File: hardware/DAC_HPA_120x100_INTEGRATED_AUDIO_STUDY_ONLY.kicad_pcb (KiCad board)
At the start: 4 copper layers, 120 x 100 mm, 544 parts, among them J101 GCT USB4105-GF-A, J201 PCB pads (no component), J202 PCB pads (no component), J701 G-Switch GT-3321667P-01, J702 HRO PJ-332A-6A, K601 TLP3545A, K602 TLP3545A, K603 TLP3545A, K604 TLP3545A, Q207 AO3400A, Q502 AO3400A, Q503 AO3400A, Q504 AO3400A, Q505 AO3400A, Q506 AO3400A, Q507 MMBT3904, Q612 MMBT3904, Q614 MMBT3904, Q616 AO3400A, Q617 AO3400A, Q618 2N7002, Q619 AO3400A, Q620 AO3400A, Q621 2N7002, Q622 AO3400A, Q623 MMBT3904, Q624 MMBT3904, Q625 MMBT3904, Q626 MMBT3904, Q627 MMBT3904, U101 ST USBLC6-2SC6, U102 TI TPS25200DRVR, U103 TI TPD2E2U06DRLR, U201 CH32V307RCT6, U202 AGRV2KQ32, U205 74LVC1G157, U206 74LVC1G11, U208 74LVC3G34, U301 ES9018K2M, U302 3.3 V, 250 mA, U303 1.300 V (R533/R534), U401 OPA1622IDRCR, U402 OPA1622IDRCR, U403 OPA2210IDGKR, U404 OPA2210IDGKR, U501 +3.85 / -3.72 V, U502 3.3 V, 150 mA, U503 TI TPS259621DDAR, U504 3.3 V, 1 A, U505 TI TMUX1101DBVR, U603 TLV1704, U604 OPA2333, U605 TLV3402, U606 TLV1704, U607 74AUP1G17, U608 74LVC1G74, U609 TLV1704, U610 TLV1704, U611 TLV1704, U612 TLV1704, U613 TLV3402, U614 TLV3402, U615 TLV3402, U616 TLV3402, U617 TLV3402, U618 TLV3402, U619 TLV3402, U620 TLV3402, U621 SN74AUP2G17DCKR, X201 80.000 MHz, X202 49.152 MHz, X203 45.1584 MHz, Y201 8 MHz

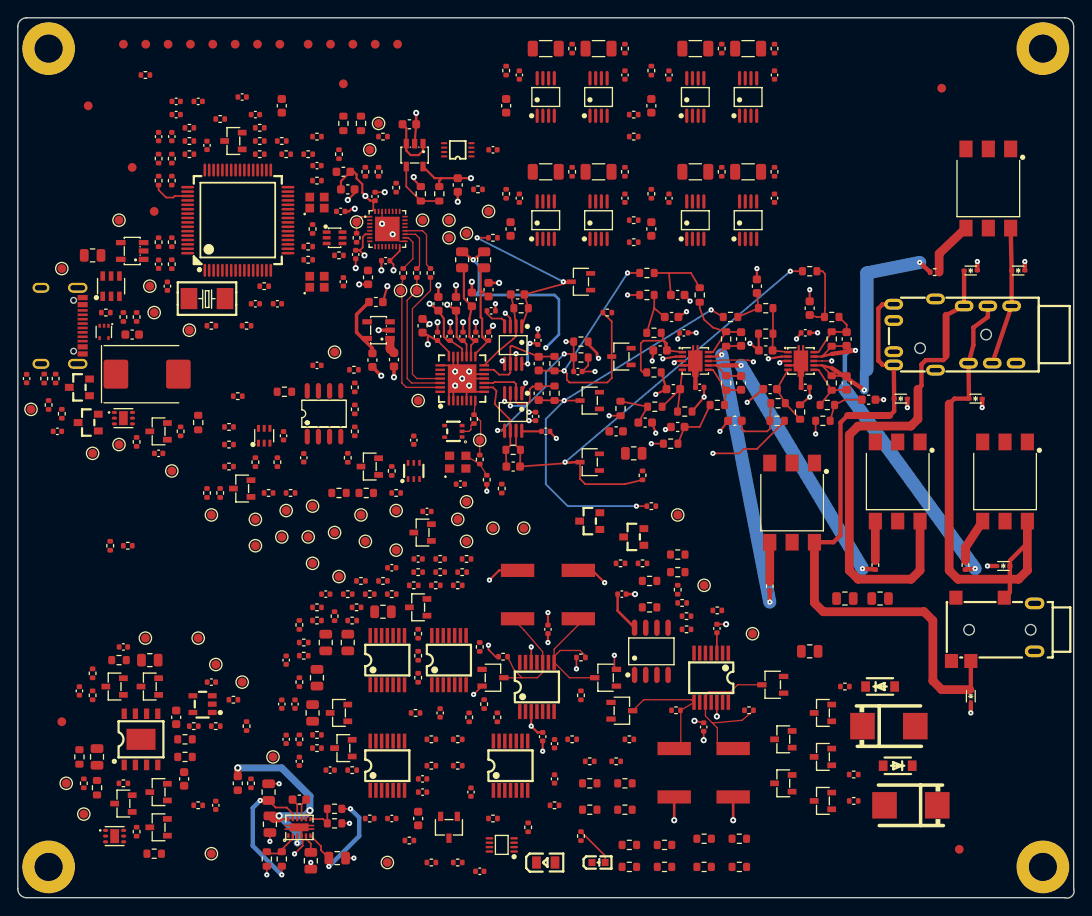
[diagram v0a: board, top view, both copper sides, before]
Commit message: feat: route power feeds, MCU fan-out and most signals on integrated board
Checkpoint of the 30 September layout pass on the 120 x 100 mm integrated
audio study (review-only, no PCBA release). CI replay passes with the
committed project settings: 0 DRC errors/warnings, 183 ratsnest links left.

- GND pours on F.Cu/L3/B.Cu in the manifest; replay refills them with
  kicad-cli so the .kicad_dru pour rules (high-Z 0.5 mm, USB 0.6 mm) hold
- 5V_SYS to U302 and the photo-relays, 5V_ANA/5V_ANA_F at 0.8 mm, VBUS,
  U201 south fan-out with VDD pins straight to their decoupling caps
- moves to clear blockages: R505, R531/C513 damper to FB501.2, R245, R703
- check_dac_core_routes counts only the two 0.7/0.3 mm 1V3 bridge vias
- new audit_return_path.py and audit_ems_layout.py screens

Co-Authored-By: Claude Opus 5.5 <noreply@anthropic.com>
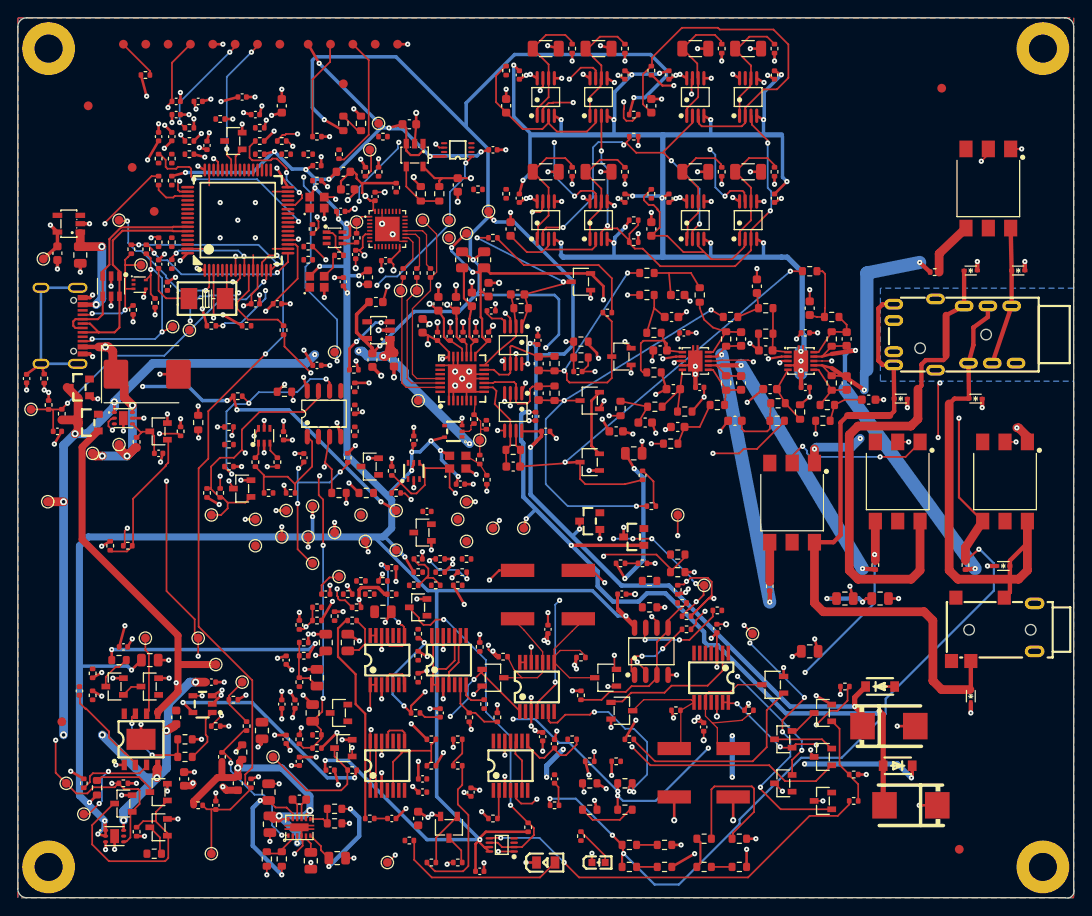
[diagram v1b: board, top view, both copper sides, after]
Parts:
- moved C513 19.0 mm to (67.8, 121.0)
- moved R531 18.5 mm to (65.5, 123.5)
- moved R104 17.9 mm to (54.6, 66.3)
- moved TP701 14.5 mm to (43.4, 95.0)
- moved TP727 14.2 mm to (57.6, 75.1)
- moved C502 12.6 mm to (44.5, 66.8), turned to -90 degrees
- moved TP703 12.5 mm to (42.9, 67.4)
- moved U502 7.84 mm to (45.8, 63.4)
- moved R103 7.72 mm to (52.9, 66.3)
- moved R703 7.46 mm to (93.2, 86.2)
- moved U103 6.75 mm to (53.9, 70.3), turned to 0 degrees
- moved TP726 5.60 mm to (54.0, 68.1)
- moved R245 5.46 mm to (70.2, 75.5), turned to 90 degrees
- moved R505 4.74 mm to (63.2, 124.0), turned to -90 degrees
- moved R102 3.94 mm to (55.6, 72.4), turned to -90 degrees
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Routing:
- net VPOS: track 93.6 -> 551.3 mm, vias 11 -> 72
- net VNEG: track 33.3 -> 407.1 mm, vias 6 -> 43
- net 3V3D: track 10.9 -> 337.2 mm, vias 0 -> 28
- net 3V3A: track 39.9 -> 306.9 mm, vias 3 -> 20
- net 3V3M: track 0.00 -> 263.0 mm, vias 0 -> 35
- net GND: track 110.7 -> 323.6 mm, vias 76 -> 261
- net 5V_SYS: track 1.51 -> 209.2 mm, vias 0 -> 16
- net LEG_RP: track 5.07 -> 156.8 mm, vias 0 -> 6
- net AUD_EN: track 0.00 -> 134.6 mm, vias 0 -> 4
- net N4_VPOS_IV: track 6.31 -> 105.4 mm, vias 2 -> 6
- net N6_SR_C: track 0.00 -> 89.7 mm, vias 0 -> 4
- net LEG_LN: track 4.49 -> 93.6 mm, vias 0 -> 9
- net N4_VNEG_IV: track 8.70 -> 93.9 mm, vias 2 -> 5
- net ANA_SENSE: track 0.00 -> 82.3 mm, vias 0 -> 2
- net ILIM_HI: track 0.00 -> 77.6 mm, vias 0 -> 7
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- added copper zone on B.Cu, net GND
- added copper zone on F.Cu, net GND
- added copper zone on In2.Cu, net GND

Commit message: feat: route to 87 ratsnest links and add EMS simulations
Second checkpoint of the integrated audio study (review-only). CI replay
passes with the committed project settings: 0 DRC errors/warnings.

- automl/rip-up passes over protection, MCU and control nets; router vias
  keep 0.8 mm from the DAC input copper so L2 stays solid under it
- R703 relocated beside the MCLK trunk, >= 2 mm from the DAC inputs
- LTspice decks: headphone-output RF ingress (TVS/relay/OPA1622 network),
  FB501 + R531/C513 damper; MATLAB EMIRR/PSRR/hum budget
- review_output_rf_filter.py: calibrated OPA1622 stability sweep of the
  proposed R417-R420 ferrite bead + LEG C0G output RF filter

Co-Authored-By: Claude Opus 5.5 <noreply@anthropic.com>
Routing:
- net LEG_RN: track 9.66 -> 172.8 mm, vias 0 -> 13
- net RELAY_EN: track 14.7 -> 143.3 mm, vias 2 -> 11
- net N6_OLN_R: track 23.7 -> 134.5 mm, vias 0 -> 5
- net N2_AVCC_EN_G: track 0.00 -> 100.6 mm, vias 0 -> 6
- net N6_OLP_L: track 34.1 -> 134.5 mm, vias 5 -> 10
- net N6_OLN_L: track 56.2 -> 152.4 mm, vias 5 -> 14
- net N6_H: track 43.1 -> 135.3 mm, vias 6 -> 14
- net N6_OLP_R: track 37.7 -> 115.6 mm, vias 3 -> 7
- net RAILS_OK_N: track 5.59 -> 76.3 mm, vias 0 -> 5
- net N6_GMC: track 68.1 -> 0.00 mm, vias 2 -> 0
- net ANA_FAULT_N: track 8.71 -> 74.8 mm, vias 0 -> 5
- net DAC_LOCK: track 0.00 -> 61.6 mm, vias 0 -> 6
- net DC_SENSE_LP: track 67.4 -> 10.1 mm, vias 4 -> 0
- net DC_SENSE_RP: track 5.94 -> 57.2 mm, vias 0 -> 3
- net I2C_SCL: track 0.00 -> 47.5 mm, vias 0 -> 5
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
